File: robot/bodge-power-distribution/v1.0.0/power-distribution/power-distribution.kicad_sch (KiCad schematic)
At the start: 5 parts, among them J1 Conn_01x02, SW1 CF-LD-1DC4-AR2W

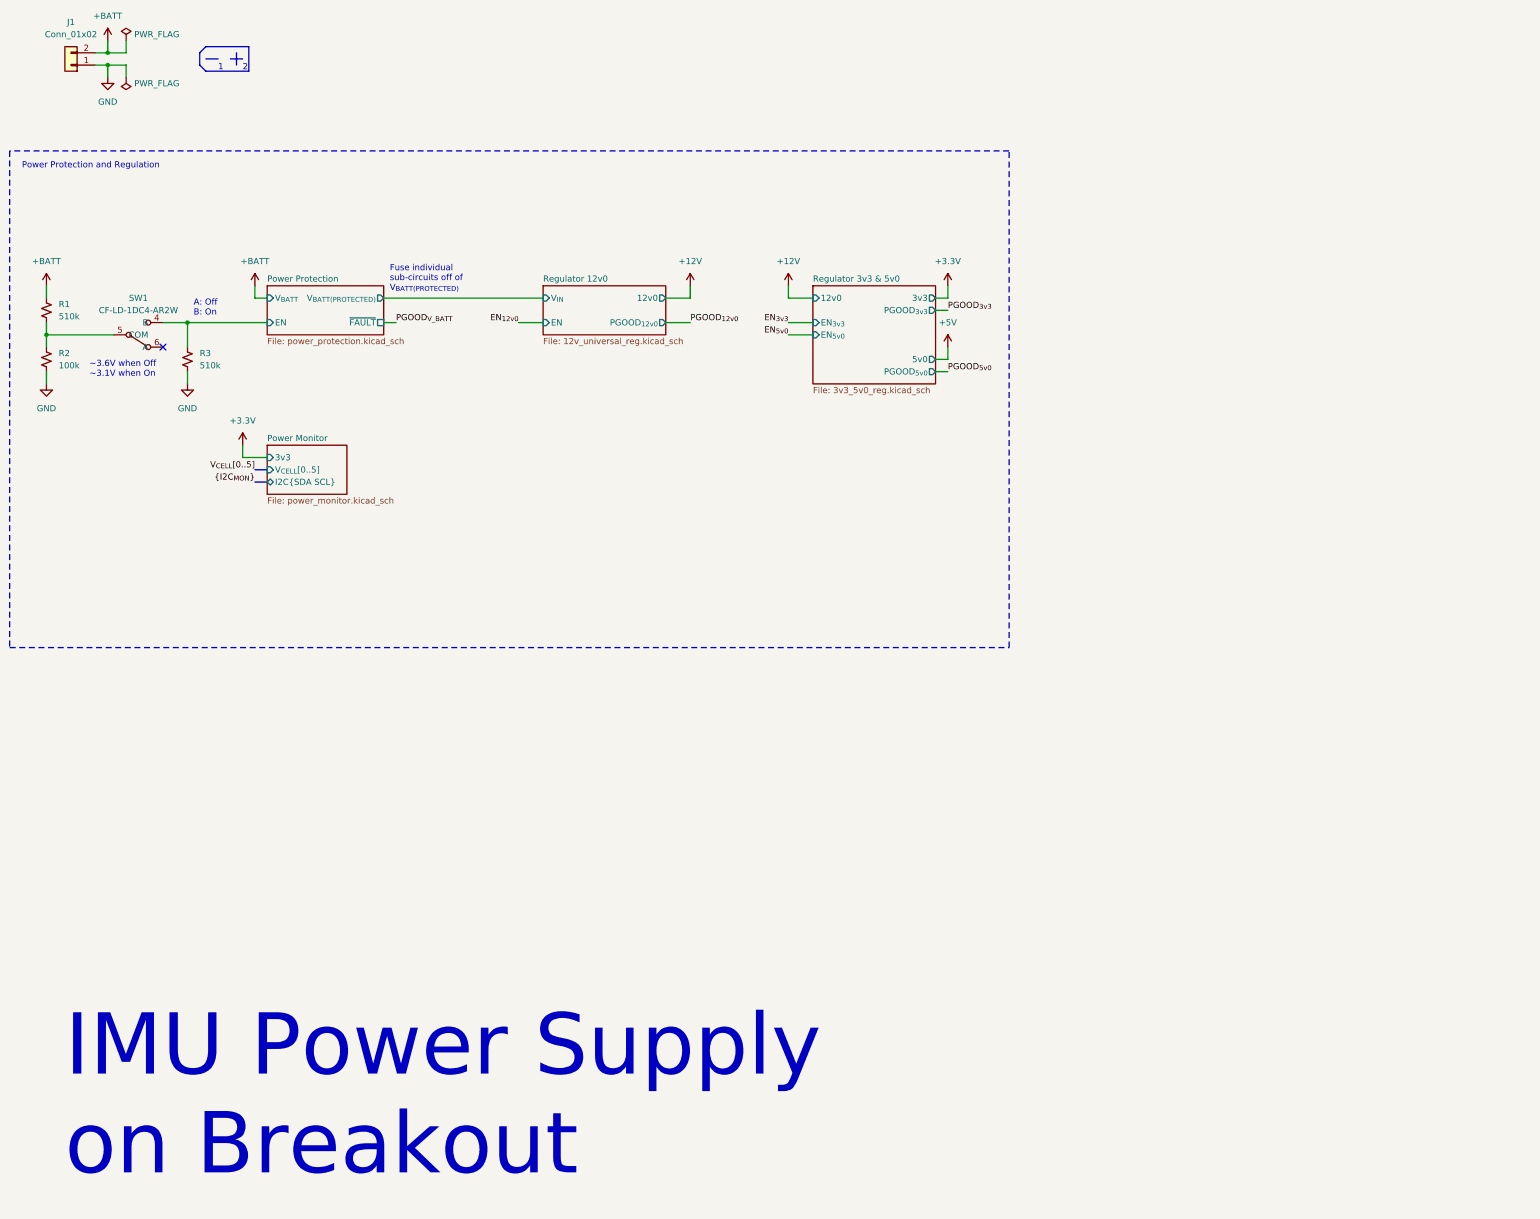
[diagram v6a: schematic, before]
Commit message: Start implementation for soft-turn off
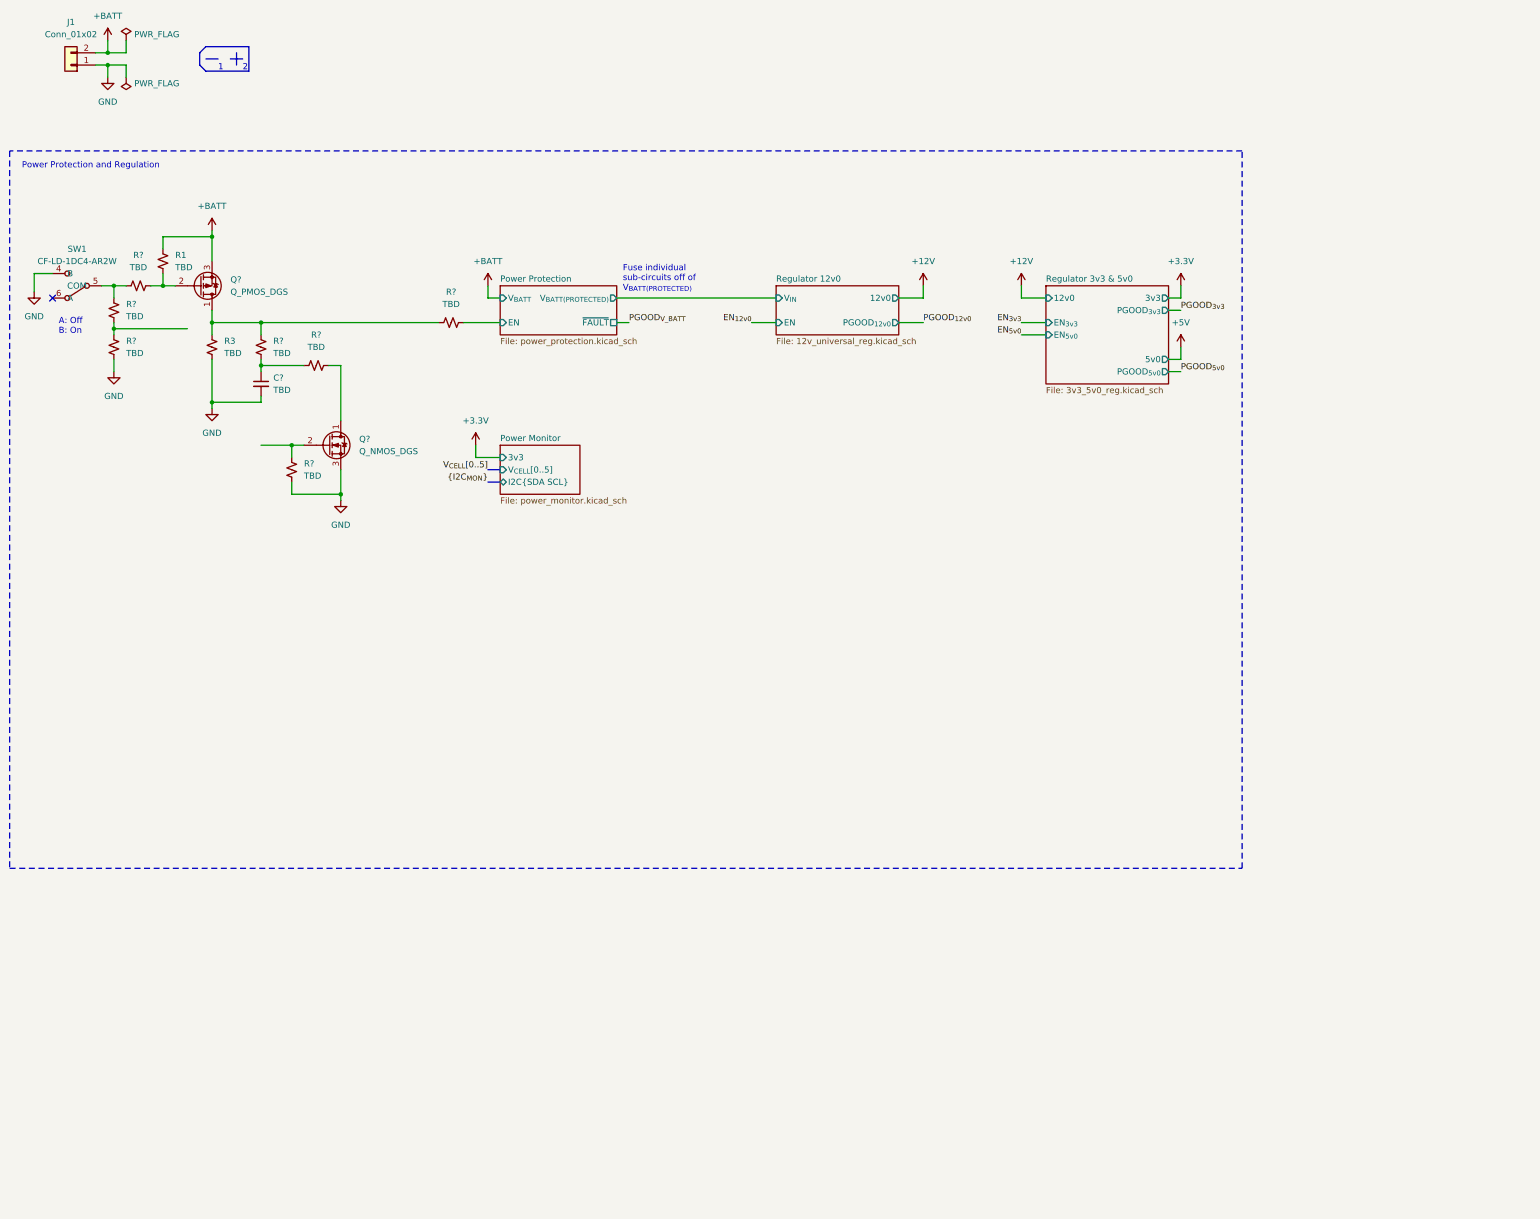
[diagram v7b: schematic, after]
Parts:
- removed R2: 100k, Resistor_SMD:R_0402_1005Metric_Pad0.72x0.64mm_HandSolder, symbol Device:R_Small_US
- added C?: TBD, symbol Device:C_Small
- added Q?: Q_PMOS_DGS, symbol Device:Q_PMOS_DGS
- added Q?: Q_NMOS_DGS, symbol Device:Q_NMOS_DGS
- added R? (x7): TBD, Resistor_SMD:R_0402_1005Metric_Pad0.72x0.64mm_HandSolder, symbol Device:R_Small_US
- R1, R3: value 510k -> TBD
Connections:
- net +BATT: now also Q?.3 (S)
- net GND: now also SW1.4 (B), C?.2, Q?.3 (S), R?.1, R?.2
- net Power Protection/EN: now also R?.2; no longer R3.1, SW1.4 (B)
- net at SW1.5 (COM): now also R?.2, R?.2; no longer R1.1
- new net: R?.1, R?.2
- new net: Q?.2 (G), R1.1, R?.1
- new net: Q?.1 (D), R3.1, R?.1, R?.1
- new net: C?.1, R?.1, R?.2
- new net: Q?.1 (D), R?.2
- new net: Q?.2 (G), R?.1
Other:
- note removed: "IMU Power Supply on Breakout"
- note removed: "~3.6V when Off ~3.1V when On"
- moved on the sheet: R1, R3, SW1

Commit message: Sync
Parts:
- R1: value TBD -> 100k
- R?: value TBD -> 10
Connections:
- net MainSwitch: now reaches R?.1, R?.2
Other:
- moved on the sheet: C?, Q?, R1, R3, R?, SW1
